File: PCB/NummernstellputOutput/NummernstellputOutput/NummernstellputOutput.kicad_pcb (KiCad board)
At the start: 2 copper layers, 65 x 76 mm, 40 parts, among them J1 Screw_Terminal_01x05, U7 MCP2561-E-P, U8 PIC18F26K83-xSP

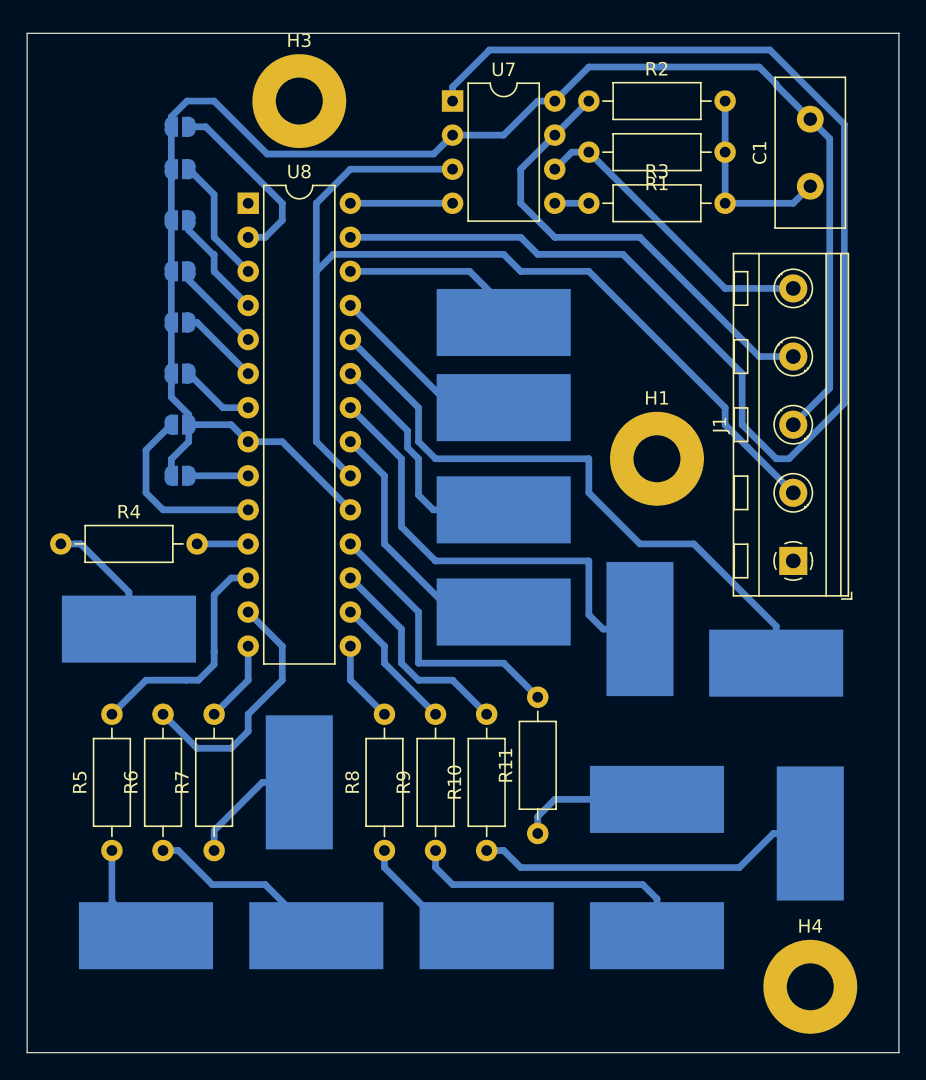
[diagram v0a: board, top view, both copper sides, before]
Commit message: Update PCBs and add track occupation PCB.
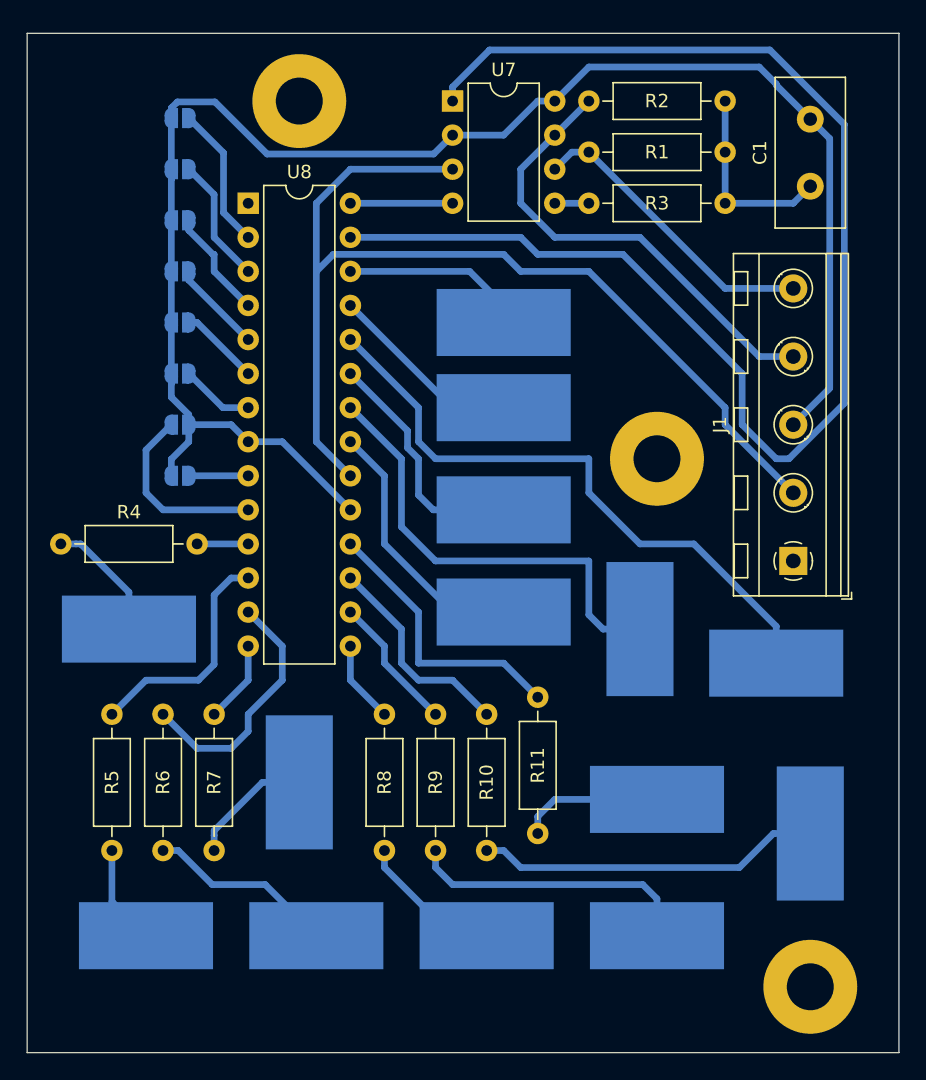
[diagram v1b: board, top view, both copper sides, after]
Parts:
- moved CANADR0 0.65 mm to (25.4, 20.3)
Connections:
- J1 pad 1: Net-(J1-Pad1) -> unconnected-(J1-Pin_1-Pad1)
- U8 pad 1: Net-(U8-Pad1) -> unconnected-(U8-VPP/~{MCLR}/RE3-Pad1)
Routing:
- net Net-(CANADR0-B): track 13.7 -> 10.7 mm
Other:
- net class Default removed
